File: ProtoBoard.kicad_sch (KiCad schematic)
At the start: 56 parts, among them J1 Conn_01x02_Female, J10 Conn_01x06_Female, J2 Conn_01x10_Female, J3 I2C_STANDARDQWIIC, J4 Conn_01x10_Female, J5 Conn_01x05_Female, J6 Conn_01x05_Female, J7 Conn_01x10_Female, J8 Conn_01x05_Female, J9 Conn_01x10_Female, Q1 2N7002, Q2 2N7002, Q3 2N7002, Q4 2N7002, Q5 2N7002, U1 ESP32-WROOM-32D, U10 SY6280AAC, U2 INA219AxD, U3 LM1084-5.0, U4 MCP3428, U5 MCP3428, U6 LM1084-3.3, U7 SY6280AAC, U8 SY6280AAC, U9 SY6280AAC

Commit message: add shunt resistor and set i2c addresses
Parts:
- added R13: 0.01R, Resistor_SMD:R_0402_1005Metric, symbol Device:R
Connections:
- net GND: now also U2.1 (A1), U2.2 (A0), U4.10 (Adr1), U4.9 (Adr0), U5.9 (Adr0)
- net at J1.2 (Pin_2): now also U2.7 (IN-), R13.2; no longer U2.8 (IN+)
- net at D2.2 (A): now also U2.8 (IN+), R13.1; no longer U2.7 (IN-)
- no-connect marks 6 -> 7
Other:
- note added: "@1101000"
- note added: "@1101001"
- note added: "Battery monitoring @1000000"
- note removed: "Battery monitoring"
- note removed: "TODO : Rshunt"
- moved on the sheet: D2, J1

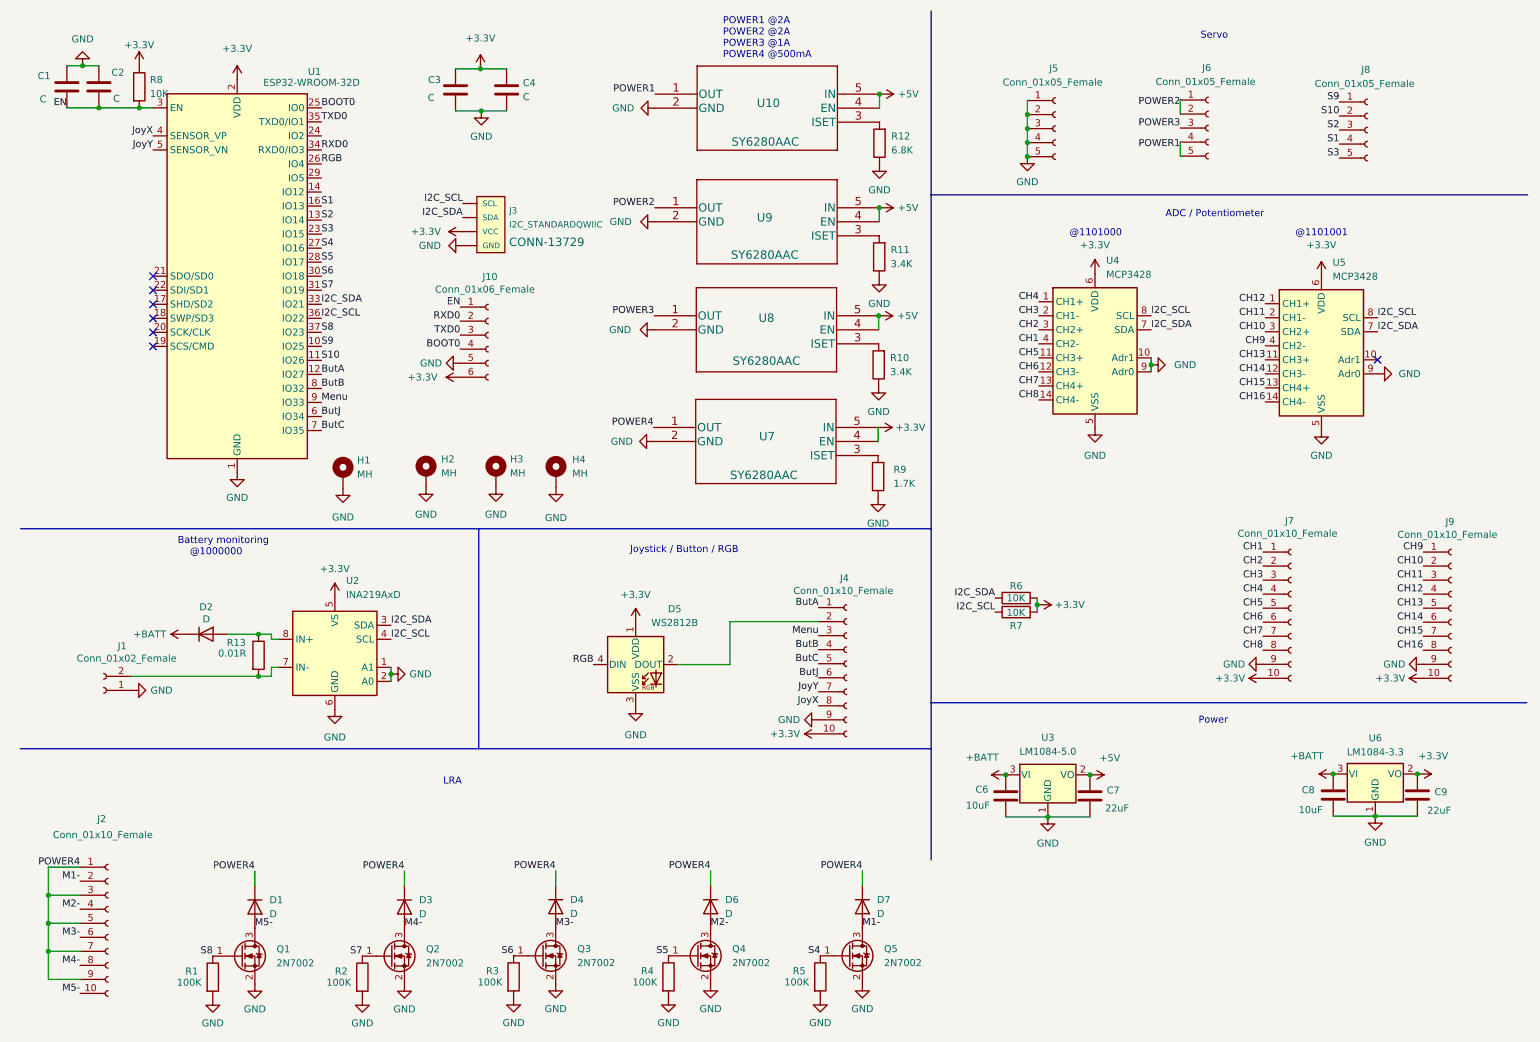
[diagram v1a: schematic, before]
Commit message: smaller (but more expensive) version board
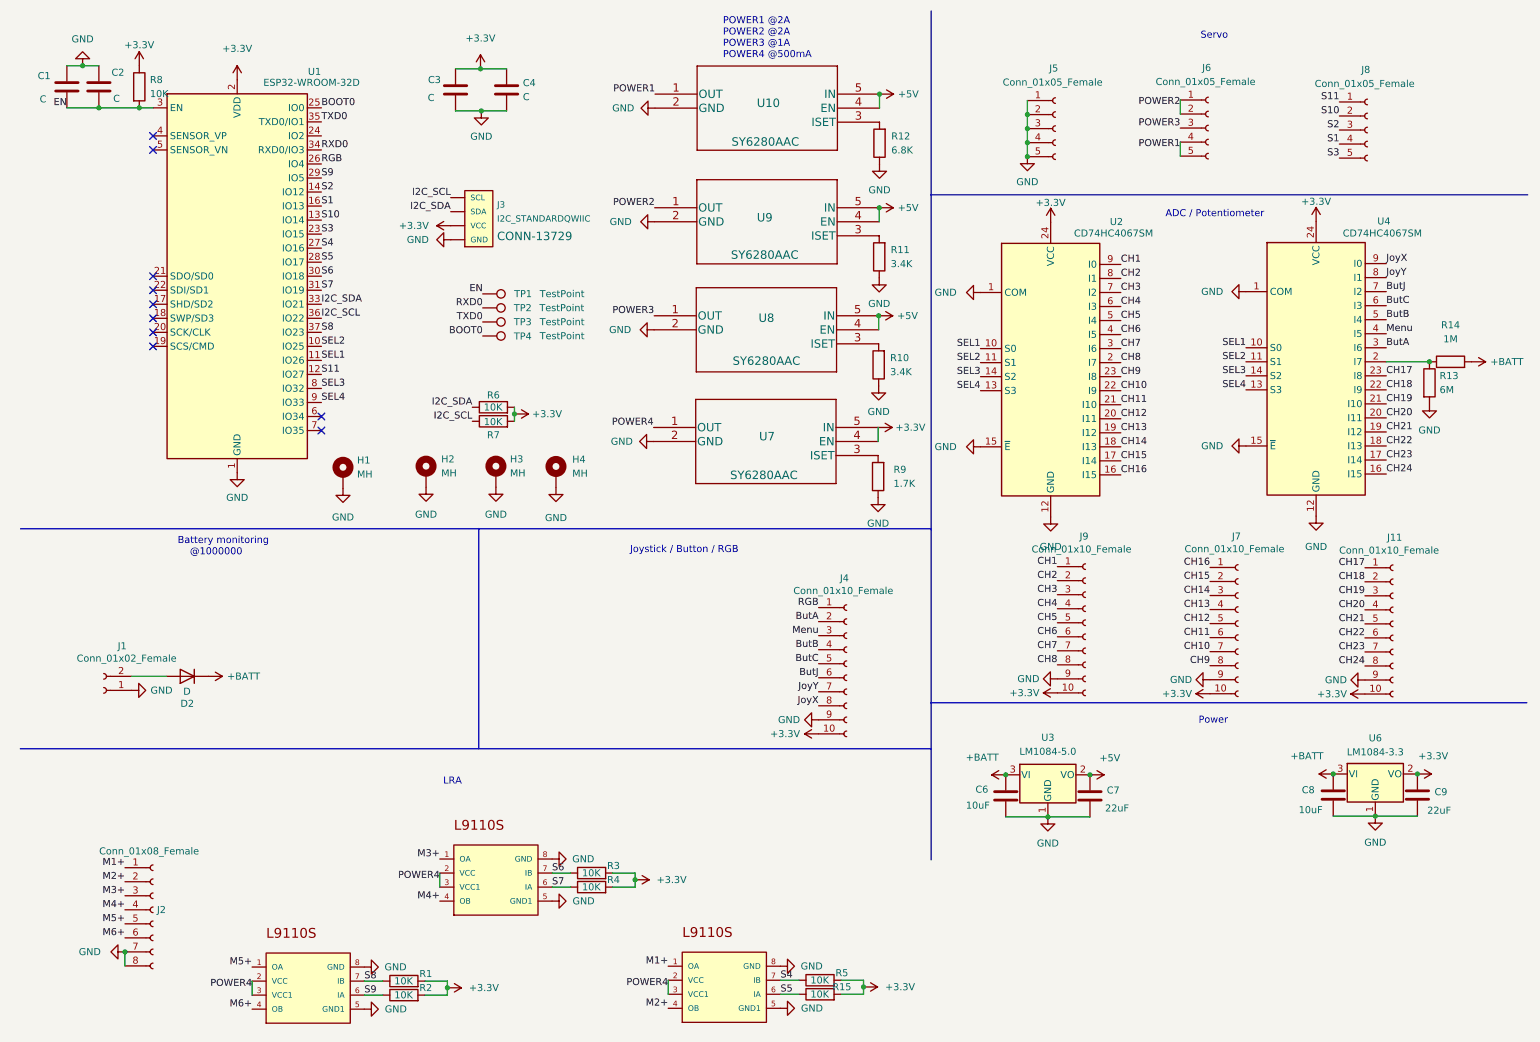
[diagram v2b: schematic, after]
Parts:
- removed D1, D3, D4, D6, D7: D, Diode_SMD:D_0402_1005Metric, symbol Device:D
- removed D5: WS2812B, LED_SMD:LED_WS2812B_PLCC4_5.0x5.0mm_P3.2mm, symbol LED:WS2812B
- removed J10: Conn_01x06_Female, Connector_PinHeader_2.54mm:PinHeader_1x06_P2.54mm_Vertical, symbol Connector:Conn_01x06_Female
- removed J2: Conn_01x10_Female, Connector_Hirose:Hirose_DF13-10P-1.25DSA_1x10_P1.25mm_Vertical, symbol Connector:Conn_01x10_Female
- removed Q1, Q2, Q3, Q4, Q5: 2N7002, Package_TO_SOT_SMD:SOT-23, symbol Transistor_FET:2N7002
- removed U2: INA219AxD, Package_SO:SOIC-8_3.9x4.9mm_P1.27mm, symbol Analog_ADC:INA219AxD
- removed U4, U5: MCP3428, Package_SO:TSSOP-14_4.4x5mm_P0.65mm, symbol Analog_ADC:MCP3428
- added IC1, IC2, IC3: L9110S, footprints:SOIC127P600X150-8, symbol L9110S:L9110S
- added J11: Conn_01x10_Female, Connector_JST:JST_GH_SM10B-GHS-TB_1x10-1MP_P1.25mm_Horizontal, symbol Connector:Conn_01x10_Female
- added J2: Conn_01x08_Female, Connector_JST:JST_GH_SM08B-GHS-TB_1x08-1MP_P1.25mm_Horizontal, symbol Connector:Conn_01x08_Female
- added R14: 1M, Resistor_SMD:R_0402_1005Metric, symbol Device:R
- added R15: 10K, Resistor_SMD:R_0402_1005Metric, symbol Device:R
- added TP1, TP2, TP3, TP4: TestPoint, TestPoint:TestPoint_Pad_D1.5mm, symbol Connector:TestPoint
- added U2, U4: CD74HC4067SM, Package_SO:SSOP-24_5.3x8.2mm_P0.65mm, symbol 74xx:CD74HC4067SM
- J4, J7, J9: footprint Connector_Hirose:Hirose_DF13-10P-1.25DSA_1x10_P1.25mm_Vertical -> Connector_JST:JST_GH_SM10B-GHS-TB_1x10-1MP_P1.25mm_Horizontal
- R1, R2, R3, R4, R5: value 100K -> 10K
- R13: value 0.01R -> 6M
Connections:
- net +3V3: now also R1.2, R2.2, R3.2, R4.2, R5.2, J11.10 (Pin_10), R15.2, U2.24 (VCC), U4.24 (VCC)
- net +BATT: now also R14.2
- net BOOT0: now also TP4.1
- net ButA: now also J4.2 (Pin_2), U4.3 (I6); no longer J4.1 (Pin_1), U1.12 (IO27)
- net ButB: now also U4.5 (I4); no longer U1.8 (IO32)
- net ButC: now also U4.6 (I3); no longer U1.7 (IO35)
- net ButJ: now also U4.7 (I2); no longer U1.6 (IO34)
- net CH1: now also J9.1 (Pin_1), U2.9 (I0); no longer J7.1 (Pin_1)
- net CH10: now also J7.7 (Pin_7), U2.22 (I9); no longer J9.2 (Pin_2)
- net CH11: now also J7.6 (Pin_6), U2.21 (I10); no longer J9.3 (Pin_3)
- net CH12: now also J7.5 (Pin_5), U2.20 (I11); no longer J9.4 (Pin_4)
- net CH13: now also J7.4 (Pin_4), U2.19 (I12); no longer J9.5 (Pin_5)
- net CH14: now also J7.3 (Pin_3), U2.18 (I13); no longer J9.6 (Pin_6)
- net CH15: now also J7.2 (Pin_2), U2.17 (I14); no longer J9.7 (Pin_7)
- net CH16: now also J7.1 (Pin_1), U2.16 (I15); no longer J9.8 (Pin_8)
- net CH2: now also J9.2 (Pin_2), U2.8 (I1); no longer J7.2 (Pin_2)
- net CH3: now also J9.3 (Pin_3), U2.7 (I2); no longer J7.3 (Pin_3)
- net CH4: now also J9.4 (Pin_4), U2.6 (I3); no longer J7.4 (Pin_4)
- net CH5: now also J9.5 (Pin_5), U2.5 (I4); no longer J7.5 (Pin_5)
- net CH6: now also J9.6 (Pin_6), U2.4 (I5); no longer J7.6 (Pin_6)
- net CH7: now also J9.7 (Pin_7), U2.3 (I6); no longer J7.7 (Pin_7)
- net CH8: now also J9.8 (Pin_8), U2.2 (I7); no longer J7.8 (Pin_8)
- net CH9: now also J7.8 (Pin_8), U2.23 (I8); no longer J9.1 (Pin_1)
- net EN: now also TP1.1
- net GND: now also R13.2, IC1.5 (GND1), IC1.8 (GND), IC2.5 (GND1), IC2.8 (GND), IC3.5 (GND1), IC3.8 (GND), J11.9 (Pin_9), J2.7 (Pin_7), J2.8 (Pin_8), U2.1 (COM), U2.12 (GND), U2.15 (~{E}), U4.1 (COM), U4.12 (GND), U4.15 (~{E}); no longer R1.2, R2.2, R3.2, R4.2, R5.2
- net JoyX: now also U4.9 (I0); no longer U1.4 (SENSOR_VP)
- net JoyY: now also U4.8 (I1); no longer U1.5 (SENSOR_VN)
- net Menu: now also U4.4 (I5); no longer U1.9 (IO33)
- net POWER4: now also IC1.2 (VCC), IC1.3 (VCC1), IC2.2 (VCC), IC2.3 (VCC1), IC3.2 (VCC), IC3.3 (VCC1)
- net RGB: now also J4.1 (Pin_1)
- net RXD0: now also TP2.1
- net S10: now also U1.13 (IO14); no longer U1.11 (IO26)
- net S2: now also U1.14 (IO12); no longer U1.13 (IO14)
- net S4: now also IC3.7 (IB)
- net S5: now also IC3.6 (IA), R15.1; no longer R4.1
- net S6: now also IC2.7 (IB)
- net S7: now also R4.1, IC2.6 (IA); no longer R2.1
- net S8: now also IC1.7 (IB)
- net S9: now also R2.1, U1.29 (IO5), IC1.6 (IA); no longer J8.1 (Pin_1), U1.10 (IO25)
- net TXD0: now also TP3.1
- net at J1.2 (Pin_2): now also D2.2 (A); no longer R13.2
- net at R13.1: now also R14.1, U4.2 (I7); no longer D2.2 (A)
- new net CH17: J11.1 (Pin_1), U4.23 (I8)
- new net CH18: J11.2 (Pin_2), U4.22 (I9)
- new net CH19: J11.3 (Pin_3), U4.21 (I10)
- new net CH20: J11.4 (Pin_4), U4.20 (I11)
- new net CH21: J11.5 (Pin_5), U4.19 (I12)
- new net CH22: J11.6 (Pin_6), U4.18 (I13)
- new net CH23: J11.7 (Pin_7), U4.17 (I14)
- new net CH24: J11.8 (Pin_8), U4.16 (I15)
- new net M1+: IC3.1 (OA), J2.1 (Pin_1)
- new net M2+: IC3.4 (OB), J2.2 (Pin_2)
- new net M3+: IC2.1 (OA), J2.3 (Pin_3)
- new net M4+: IC2.4 (OB), J2.4 (Pin_4)
- new net M5+: IC1.1 (OA), J2.5 (Pin_5)
- new net M6+: IC1.4 (OB), J2.6 (Pin_6)
- new net S11: J8.1 (Pin_1), U1.12 (IO27)
- new net SEL1: U1.11 (IO26), U2.10 (S0), U4.10 (S0)
- new net SEL2: U1.10 (IO25), U2.11 (S1), U4.11 (S1)
- new net SEL3: U1.8 (IO32), U2.14 (S2), U4.14 (S2)
- new net SEL4: U1.9 (IO33), U2.13 (S3), U4.13 (S3)
- no-connect marks 7 -> 10
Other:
- note removed: "@1101000"
- note removed: "@1101001"
- moved on the sheet: D2, J3, J7, J9, R6, R7

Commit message: More pcb cleaning
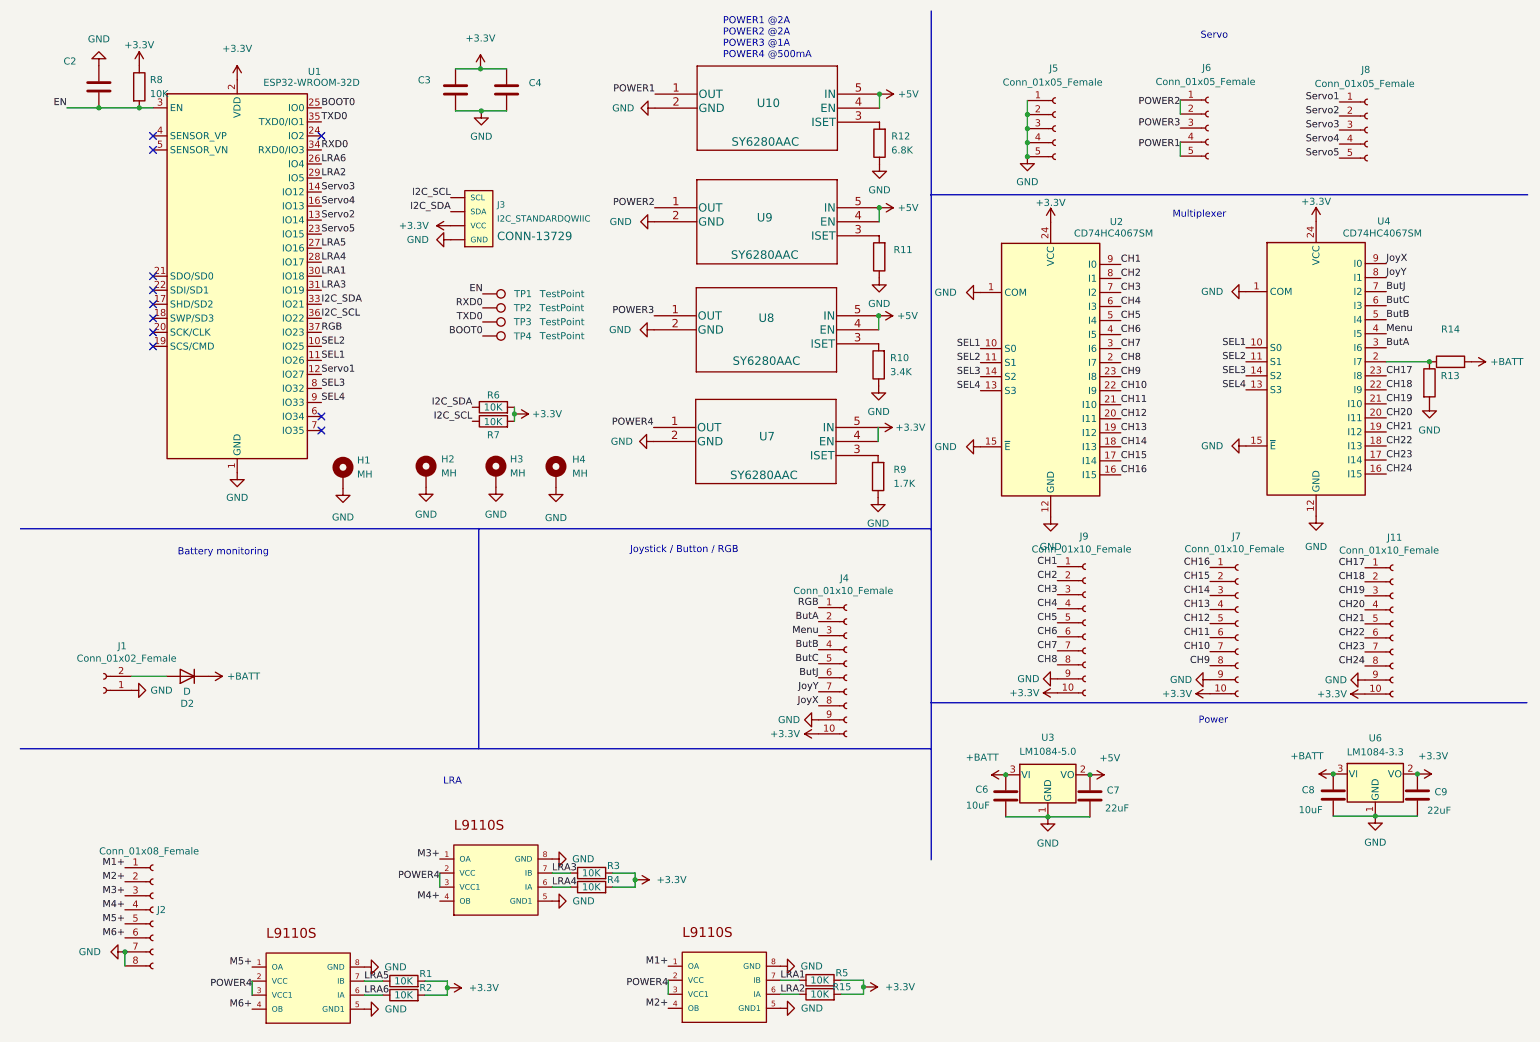
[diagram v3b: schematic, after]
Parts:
- removed C1: C, Capacitor_SMD:C_0402_1005Metric, symbol Device:C
- C2, C3, C4: value C -> (none)
- R11: value 3.4K -> (none)
- R13: value 6M -> (none)
- R14: value 1M -> (none)
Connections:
- net RGB: now also U1.37 (IO23); no longer U1.26 (IO4)
- net S1 renamed Servo4
- net S10 renamed Servo2
- net S11 renamed Servo1
- net S2 renamed Servo3
- net S3 renamed Servo5
- net S4 renamed LRA1
- net LRA1: now also U1.30 (IO18); no longer U1.27 (IO16)
- net S5 renamed LRA2
- net LRA2: now also U1.29 (IO5); no longer U1.28 (IO17)
- net S6 renamed LRA3
- net LRA3: now also U1.31 (IO19); no longer U1.30 (IO18)
- net S7 renamed LRA4
- net LRA4: now also U1.28 (IO17); no longer U1.31 (IO19)
- net S8 renamed LRA5
- net LRA5: now also U1.27 (IO16); no longer U1.37 (IO23)
- net S9 renamed LRA6
- net LRA6: now also U1.26 (IO4); no longer U1.29 (IO5)
- no-connect marks 10 -> 11
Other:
- note added: "Battery monitoring"
- note added: "Multiplexer"
- note removed: "ADC / Potentiometer"
- note removed: "Battery monitoring @1000000"
